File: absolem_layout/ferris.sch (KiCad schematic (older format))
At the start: 102 parts, among them J1 USB C, K0_0 KEYSW, K0_1 KEYSW, K0_2 KEYSW, K0_3 KEYSW, K0_4 KEYSW, K0_5 KEYSW, K0_6 KEYSW, K0_7 KEYSW, K0_8 KEYSW, K0_9 KEYSW, K1_0 KEYSW, K1_1 KEYSW, K1_2 KEYSW, K1_3 KEYSW, K1_4 KEYSW, K1_5 KEYSW, K1_6 KEYSW, K1_7 KEYSW, K1_8 KEYSW, K1_9 KEYSW, K2_0 KEYSW, K2_1 KEYSW, K2_2 KEYSW, K2_3 KEYSW, K2_4 KEYSW, K2_5 KEYSW, K2_6 KEYSW, K2_7 KEYSW, K2_8 KEYSW, K2_9 KEYSW, K3_2 KEYSW, K3_3 KEYSW, K3_4 KEYSW, K3_5 KEYSW, K3_6 KEYSW, K3_7 KEYSW, SW1 SW_PUSH, U1 ATmega32U4-AU, Y1 Crystal

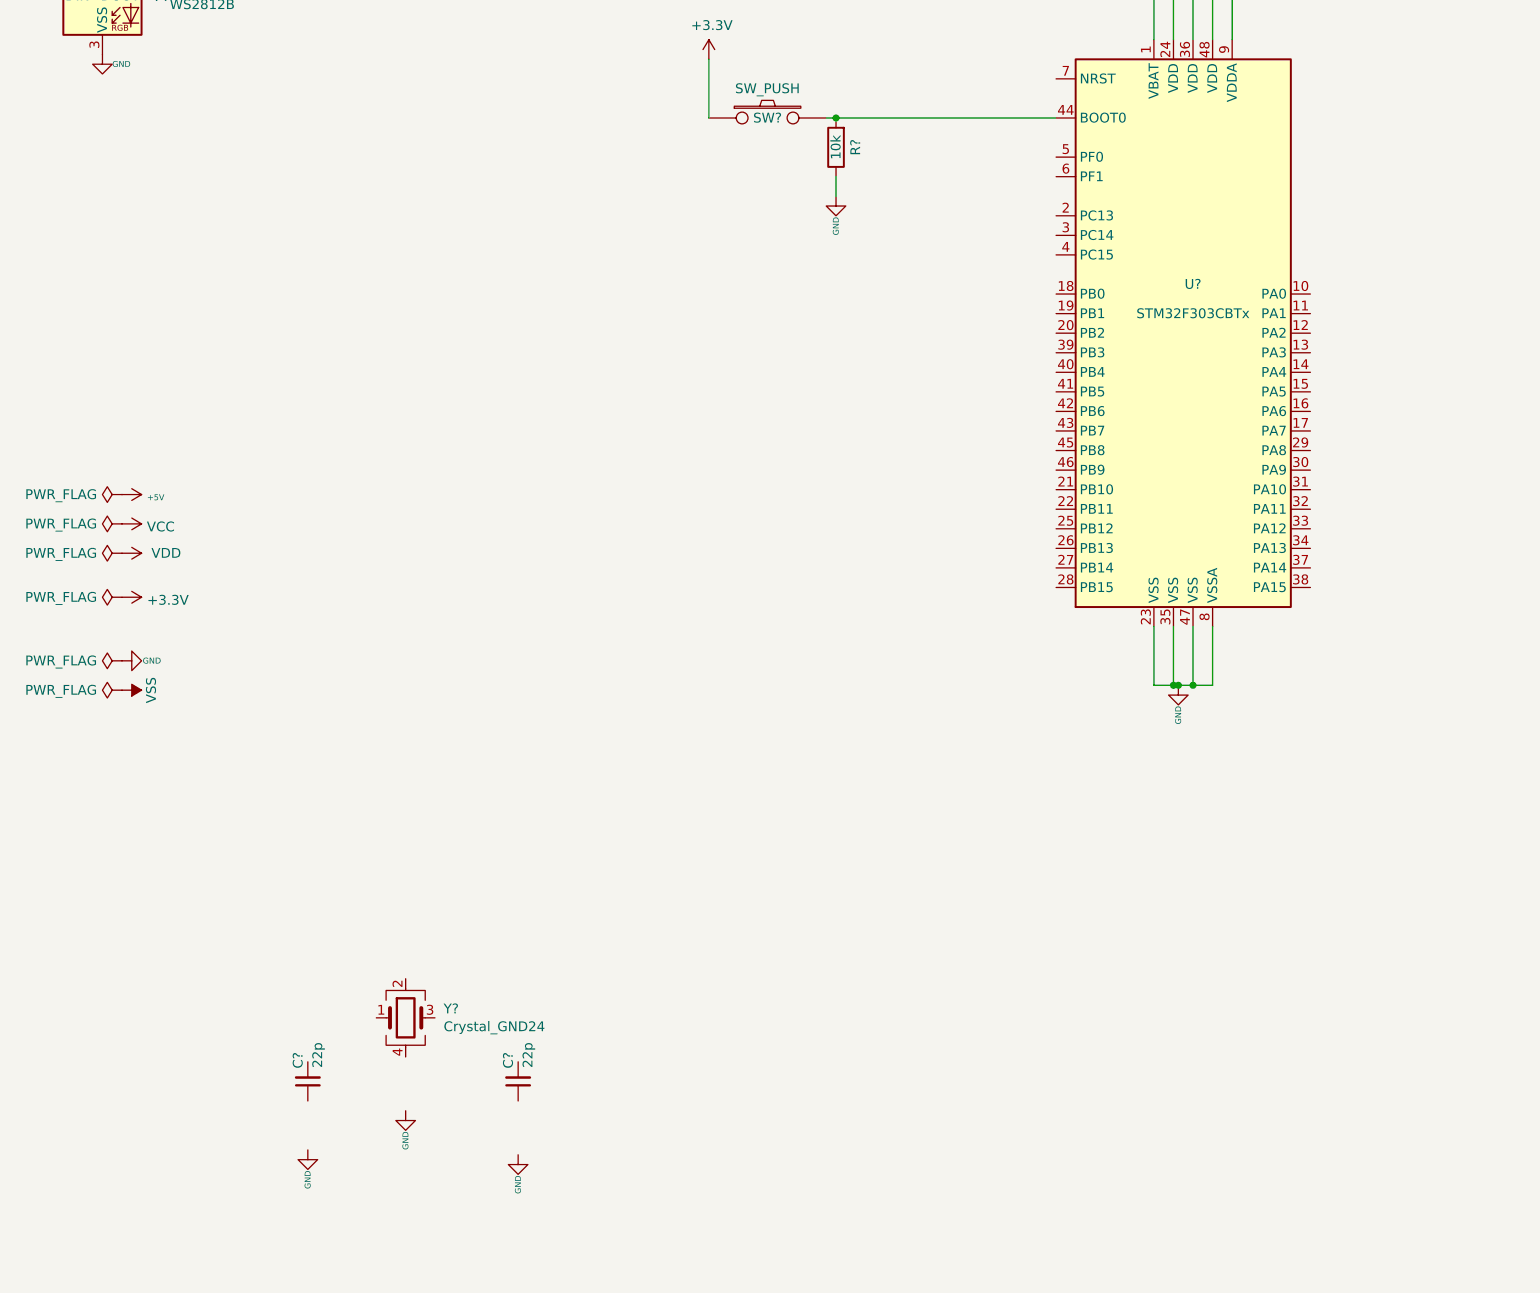
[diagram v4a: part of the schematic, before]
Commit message: Oscillator added to the schematic.
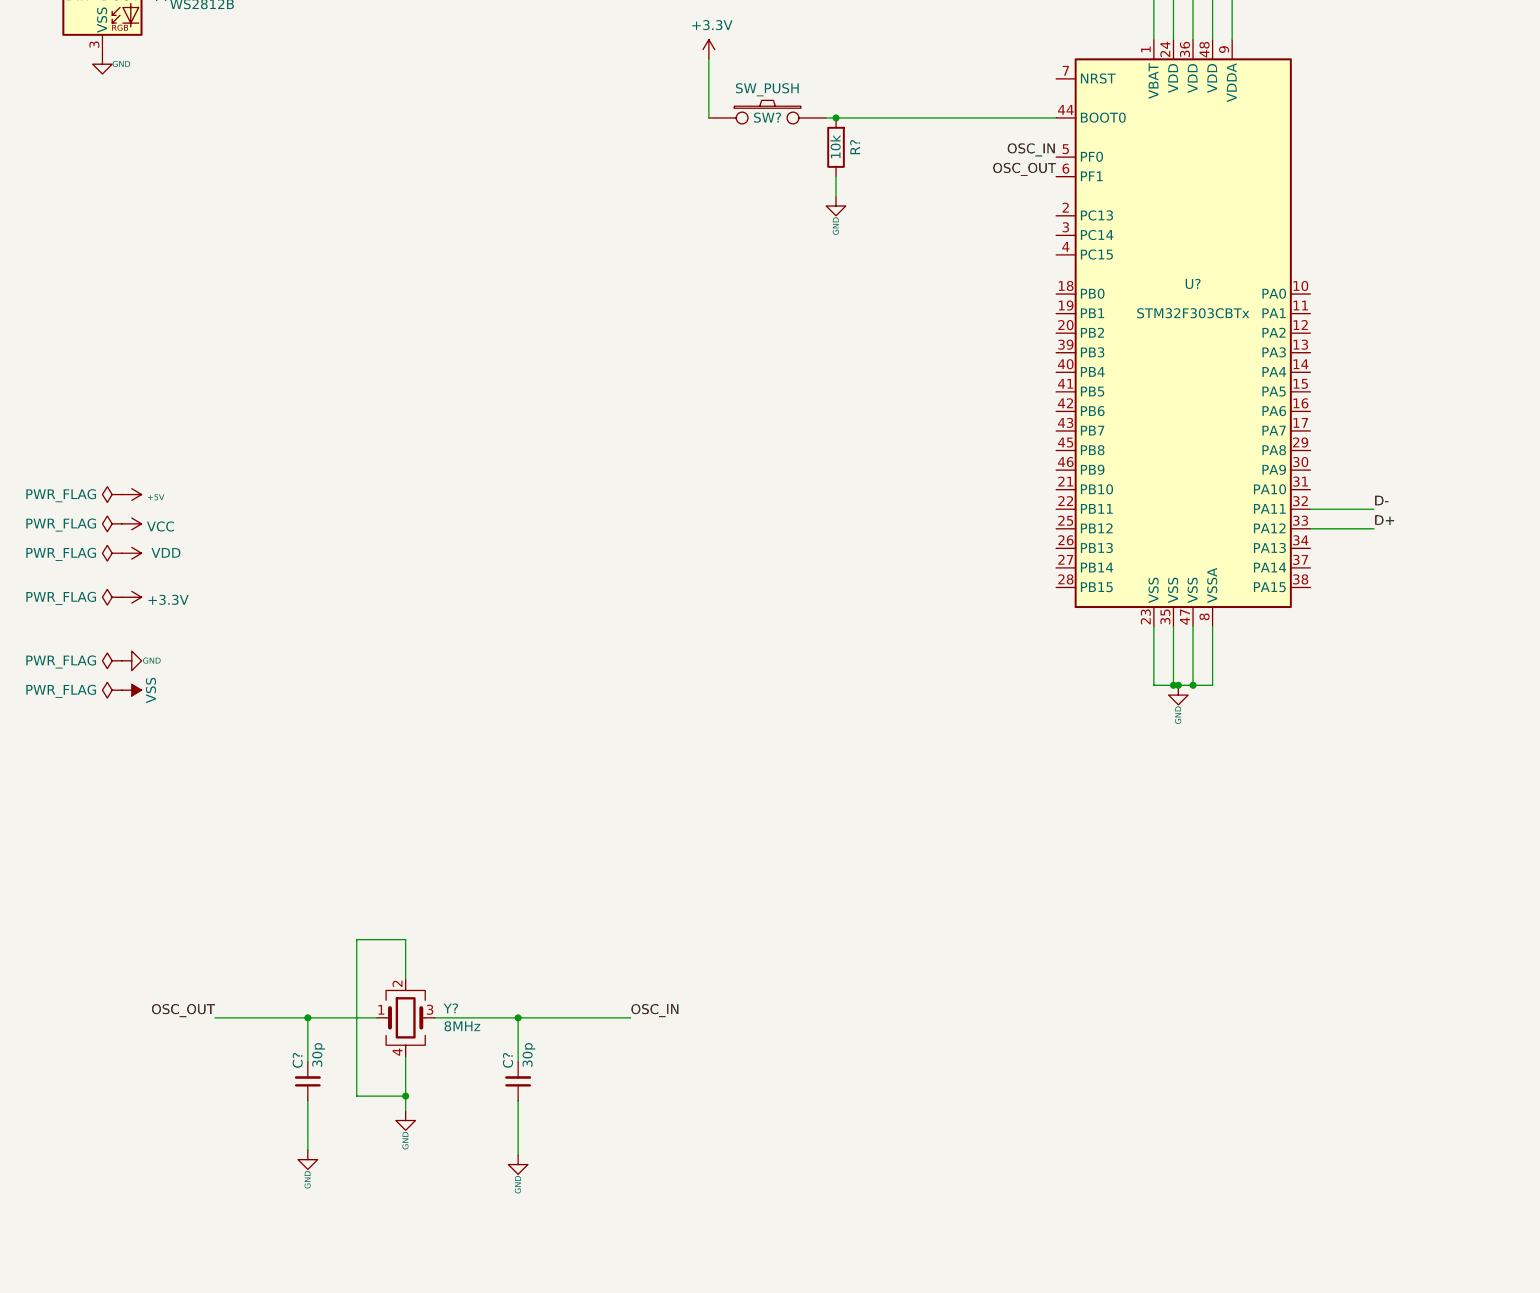
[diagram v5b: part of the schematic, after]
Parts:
- C? (x2): value 22p -> 30p
- Y?: value Crystal_GND24 -> 8MHz; footprint (none) -> Crystal:Crystal_SMD_5032-4Pin_5.0x3.2mm
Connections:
- net D+: now also U?.33 (PA12)
- net D-: now also U?.32 (PA11)
- net GND: now also C?.1, C?.1, Y?.2, Y?.4
- net OSC_IN: now reaches U?.5 (PF0)
- net OSC_IN: now also C?.2, Y?.3
- net OSC_OUT: now reaches U?.6 (PF1)
- net OSC_OUT: now also C?.2, Y?.1
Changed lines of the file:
@@
 P 6800 8925
 F 0 "Y?" H 6994 8971 50  0000 L CNN
-F 1 "Crystal_GND24" H 6994 8880 50  0000 L CNN
-F 2 "" H 6800 8925 50  0001 C CNN
+F 1 "8MHz" H 6994 8880 50  0000 L CNN
+F 2 "Crystal:Crystal_SMD_5032-4Pin_5.0x3.2mm" H 6800 8925 50  0001 C CNN
 F 3 "~" H 6800 8925 50  0001 C CNN
 	1    6800 8925
@@
 P 6300 9250
 F 0 "C?" V 6350 9100 50  0000 L CNN
-F 1 "22p" V 6250 9050 50  0000 L CNN
+F 1 "30p" V 6250 9050 50  0000 L CNN
 F 2 "Capacitor_SMD:C_0805_2012Metric_Pad1.15x1.40mm_HandSolder" H 6300 9250 50  0001 C CNN
 F 3 "~" H 6300 9250 50  0001 C CNN
@@
 P 7375 9250
 F 0 "C?" V 7425 9100 50  0000 L CNN
-F 1 "22p" V 7325 9050 50  0000 L CNN
+F 1 "30p" V 7325 9050 50  0000 L CNN
 F 2 "Capacitor_SMD:C_0805_2012Metric_Pad1.15x1.40mm_HandSolder" H 7375 9250 50  0001 C CNN
 F 3 "~" H 7375 9250 50  0001 C CNN
@@
 	1    0    0    -1
 $EndComp
+Text Label 10125 4525 2    50   ~ 0
+OSC_IN
+Text Label 10125 4625 2    50   ~ 0
+OSC_OUT
+Text Label 5825 8925 2    50   ~ 0
+OSC_OUT
+Text Label 7950 8925 0    50   ~ 0
+OSC_IN
+Wire Wire Line
+	7950 8925 7375 8925
+Wire Wire Line
+	6650 8925 6300 8925
+Wire Wire Line
+	6300 9150 6300 8925
+Connection ~ 6300 8925
+Wire Wire Line
+	6300 8925 5825 8925
+Wire Wire Line
+	6300 9350 6300 9600
+Wire Wire Line
+	7375 9150 7375 8925
+Connection ~ 7375 8925
+Wire Wire Line
+	7375 8925 6950 8925
+Wire Wire Line
+	7375 9350 7375 9625
+Wire Wire Line
+	6800 9125 6800 9325
+Wire Wire Line
+	6800 8725 6800 8525
+Wire Wire Line
+	6800 8525 6550 8525
+Wire Wire Line
+	6550 8525 6550 9325
+Wire Wire Line
+	6550 9325 6800 9325
+Connection ~ 6800 9325
+Wire Wire Line
+	6800 9325 6800 9400
+Text Label 11750 6425 0    50   ~ 0
+D+
+Text Label 11750 6325 0    50   ~ 0
+D-
+Wire Wire Line
+	11425 6325 11750 6325
+Wire Wire Line
+	11750 6425 11425 6425
 $EndSCHEMATC

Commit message: Labelling
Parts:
- gave numbers to parts that had none: 10
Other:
- note added: "EMI/RFI Filter unit"
- note added: "Oscillator unit"
- note added: "Voltage Regulator"
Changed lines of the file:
@@
 Connection ~ 3650 3900
 $Comp
-L NUF2221W1T2G:NUF2221W1T2G IC?
+L NUF2221W1T2G:NUF2221W1T2G IC1
 U 1 1 5F2F5E67
 P 1475 10250
-F 0 "IC?" H 1475 10250 50  0001 L BNN
+F 0 "IC1" H 1475 10250 50  0001 L BNN
 F 1 "NUF2221W1T2G" H 1475 10250 50  0001 L BNN
 F 2 "SOT-363" H 1475 10250 50  0001 L BNN
@@
 D-I
 $Comp
-L Regulator_Linear:TLV70012_SOT23-5 U?
+L Regulator_Linear:TLV70012_SOT23-5 U2
 U 1 1 5F305548
 P 3825 9875
-F 0 "U?" H 3825 10217 50  0000 C CNN
+F 0 "U2" H 3825 10217 50  0000 C CNN
 F 1 "TLV70012_SOT23-5" H 3825 10126 50  0000 C CNN
 F 2 "Package_TO_SOT_SMD:SOT-23-5" H 3825 10200 50  0001 C CIN
@@
 $EndComp
 $Comp
-L power:+5V #PWR?
+L power:+5V #PWR0106
 U 1 1 5F308B1A
 P 3200 9625
-F 0 "#PWR?" H 3200 9595 20  0001 C CNN
+F 0 "#PWR0106" H 3200 9595 20  0001 C CNN
 F 1 "+5V" V 3215 9753 30  0000 L CNN
 F 2 "" H 3200 9625 60  0000 C CNN
@@
 $EndComp
 $Comp
-L Device:C_Small C?
+L Device:C_Small C9
 U 1 1 5F3097C9
 P 3200 10250
-F 0 "C?" V 3100 10200 50  0000 L CNN
+F 0 "C9" V 3100 10200 50  0000 L CNN
 F 1 "1u" V 3300 10150 50  0000 L CNN
 F 2 "Capacitor_SMD:C_0805_2012Metric_Pad1.15x1.40mm_HandSolder" H 3200 10250 50  0001 C CNN
@@
 $EndComp
 $Comp
-L Device:C_Small C?
+L Device:C_Small C10
 U 1 1 5F30A45A
 P 4500 10225
-F 0 "C?" V 4400 10175 50  0000 L CNN
+F 0 "C10" V 4400 10175 50  0000 L CNN
 F 1 "1u" V 4600 10125 50  0000 L CNN
 F 2 "Capacitor_SMD:C_0805_2012Metric_Pad1.15x1.40mm_HandSolder" H 4500 10225 50  0001 C CNN
@@
 $EndComp
 $Comp
-L power:GND #PWR?
+L power:GND #PWR0112
 U 1 1 5F30ABDF
 P 3825 10725
-F 0 "#PWR?" H 3825 10775 20  0001 C CNN
+F 0 "#PWR0112" H 3825 10775 20  0001 C CNN
 F 1 "GND" V 3825 10525 30  0000 L CNN
 F 2 "" H 3825 10725 60  0000 C CNN
@@
 $EndComp
 $Comp
-L power:+3.3V #PWR?
+L power:+3.3V #PWR0117
 U 1 1 5F30C6C4
 P 5350 6775
-F 0 "#PWR?" H 5350 6625 50  0001 C CNN
+F 0 "#PWR0117" H 5350 6625 50  0001 C CNN
 F 1 "+3.3V" V 5365 6903 50  0000 L CNN
 F 2 "" H 5350 6775 50  0001 C CNN
@@
 $EndComp
 $Comp
-L power:PWR_FLAG #FLG?
+L power:PWR_FLAG #FLG0106
 U 1 1 5F30D7CC
 P 5350 6775
-F 0 "#FLG?" H 5350 6850 50  0001 C CNN
+F 0 "#FLG0106" H 5350 6850 50  0001 C CNN
 F 1 "PWR_FLAG" V 5350 6902 50  0000 L CNN
 F 2 "" H 5350 6775 50  0001 C CNN
@@
 $EndComp
 $Comp
-L power:+3.3V #PWR?
+L power:+3.3V #PWR0120
 U 1 1 5F30EBCB
 P 4500 9625
-F 0 "#PWR?" H 4500 9475 50  0001 C CNN
+F 0 "#PWR0120" H 4500 9475 50  0001 C CNN
 F 1 "+3.3V" H 4515 9798 50  0000 C CNN
 F 2 "" H 4500 9625 50  0001 C CNN
@@
 D-
 $Comp
-L power:+3.3V #PWR?
+L power:+3.3V #PWR0121
 U 1 1 5F335F51
 P 1075 10150
-F 0 "#PWR?" H 1075 10000 50  0001 C CNN
+F 0 "#PWR0121" H 1075 10000 50  0001 C CNN
 F 1 "+3.3V" V 1090 10278 50  0000 L CNN
 F 2 "" H 1075 10150 50  0001 C CNN
@@
 $EndComp
 $Comp
-L power:GND #PWR?
+L power:GND #PWR0123
 U 1 1 5F336B78
 P 1075 10650
-F 0 "#PWR?" H 1075 10700 20  0001 C CNN
+F 0 "#PWR0123" H 1075 10700 20  0001 C CNN
 F 1 "GND" V 1075 10450 30  0000 L CNN
 F 2 "" H 1075 10650 60  0000 C CNN
@@
 $EndComp
 $Comp
-L MCU_ST_STM32F3:STM32F303CBTx U?
+L MCU_ST_STM32F3:STM32F303CBTx U3
 U 1 1 5F2CE539
 P 10825 5425
-F 0 "U?" H 10825 5675 50  0000 C CNN
+F 0 "U3" H 10825 5675 50  0000 C CNN
 F 1 "STM32F303CBTx" H 10825 5525 50  0000 C CNN
 F 2 "Package_QFP:LQFP-48_7x7mm_P0.5mm" H 10225 4025 50  0001 R CNN
@@
 $EndComp
 $Comp
-L power:+3.3V #PWR?
+L power:+3.3V #PWR0124
 U 1 1 5F2D5F54
 P 10825 3500
-F 0 "#PWR?" H 10825 3350 50  0001 C CNN
+F 0 "#PWR0124" H 10825 3350 50  0001 C CNN
 F 1 "+3.3V" H 10840 3673 50  0000 C CNN
 F 2 "" H 10825 3500 50  0001 C CNN
@@
 Connection ~ 10725 3650
 $Comp
-L power:GND #PWR?
+L power:GND #PWR0125
 U 1 1 5F30895E
-P 10750 7225
-F 0 "#PWR?" H 10750 7275 20  0001 C CNN
-F 1 "GND" V 10750 7025 30  0000 L CNN
-F 2 "" H 10750 7225 60  0000 C CNN
-F 3 "" H 10750 7225 60  0000 C CNN
-	1    10750 7225
+P 10750 7400
+F 0 "#PWR0125" H 10750 7450 20  0001 C CNN
+F 1 "GND" V 10750 7200 30  0000 L CNN
+F 2 "" H 10750 7400 60  0000 C CNN
+F 3 "" H 10750 7400 60  0000 C CNN
+	1    10750 7400
 	1    0    0    -1
 $EndComp
@@
 	10825 7225 10750 7225
 $Comp
-L ferris-rescue:SW_PUSH-keyboard_parts-ferris-rescue SW?
+L ferris-rescue:SW_PUSH-keyboard_parts-ferris-rescue SW2
 U 1 1 5F33508A
 P 8650 4325
-F 0 "SW?" H 8650 4325 50  0000 C CNN
+F 0 "SW2" H 8650 4325 50  0000 C CNN
 F 1 "SW_PUSH" H 8650 4475 50  0000 C CNN
 F 2 "Button_Switch_SMD:SW_SPST_B3U-1000P" H 8650 4325 60  0001 C CNN
@@
 	10125 4325 9000 4325
 $Comp
-L power:+3.3V #PWR?
+L power:+3.3V #PWR0126
 U 1 1 5F346246
 P 8350 4025
-F 0 "#PWR?" H 8350 3875 50  0001 C CNN
+F 0 "#PWR0126" H 8350 3875 50  0001 C CNN
 F 1 "+3.3V" H 8365 4198 50  0000 C CNN
 F 2 "" H 8350 4025 50  0001 C CNN
@@
 	8350 4025 8350 4325
 $Comp
-L Device:R R?
+L Device:R R7
 U 1 1 5F355C69
 P 9000 4475
-F 0 "R?" V 8900 4475 50  0000 C CNN
+F 0 "R7" V 8900 4475 50  0000 C CNN
 F 1 "10k" V 9000 4475 50  0000 C CNN
 F 2 "Resistor_SMD:R_0805_2012Metric_Pad1.15x1.40mm_HandSolder" V 8930 4475 50  0001 C CNN
@@
 	9000 4325 8950 4325
 $Comp
-L power:GND #PWR?
+L power:GND #PWR0130
 U 1 1 5F359ECB
 P 9000 4725
-F 0 "#PWR?" H 9000 4775 20  0001 C CNN
+F 0 "#PWR0130" H 9000 4775 20  0001 C CNN
 F 1 "GND" V 9000 4525 30  0000 L CNN
 F 2 "" H 9000 4725 60  0000 C CNN
@@
 	9000 4625 9000 4725
 $Comp
-L Device:Crystal_GND24 Y?
+L Device:Crystal_GND24 Y2
 U 1 1 5F3648C6
 P 6800 8925
-F 0 "Y?" H 6994 8971 50  0000 L CNN
+F 0 "Y2" H 6994 8971 50  0000 L CNN
 F 1 "8MHz" H 6994 8880 50  0000 L CNN
 F 2 "Crystal:Crystal_SMD_5032-4Pin_5.0x3.2mm" H 6800 8925 50  0001 C CNN
@@
 $EndComp
 $Comp
-L Device:C_Small C?
+L Device:C_Small C11
 U 1 1 5F388BCB
 P 6300 9250
-F 0 "C?" V 6350 9100 50  0000 L CNN
+F 0 "C11" V 6350 9100 50  0000 L CNN
 F 1 "30p" V 6250 9050 50  0000 L CNN
 F 2 "Capacitor_SMD:C_0805_2012Metric_Pad1.15x1.40mm_HandSolder" H 6300 9250 50  0001 C CNN
@@
 $EndComp
 $Comp
-L Device:C_Small C?
+L Device:C_Small C12
 U 1 1 5F3901A1
 P 7375 9250
-F 0 "C?" V 7425 9100 50  0000 L CNN
+F 0 "C12" V 7425 9100 50  0000 L CNN
 F 1 "30p" V 7325 9050 50  0000 L CNN
 F 2 "Capacitor_SMD:C_0805_2012Metric_Pad1.15x1.40mm_HandSolder" H 7375 9250 50  0001 C CNN
@@
 $EndComp
 $Comp
-L power:GND #PWR?
+L power:GND #PWR0131
 U 1 1 5F391618
 P 6300 9600
-F 0 "#PWR?" H 6300 9650 20  0001 C CNN
+F 0 "#PWR0131" H 6300 9650 20  0001 C CNN
 F 1 "GND" V 6300 9400 30  0000 L CNN
 F 2 "" H 6300 9600 60  0000 C CNN
@@
 $EndComp
 $Comp
-L power:GND #PWR?
+L power:GND #PWR0132
 U 1 1 5F392713
 P 7375 9625
-F 0 "#PWR?" H 7375 9675 20  0001 C CNN
+F 0 "#PWR0132" H 7375 9675 20  0001 C CNN
 F 1 "GND" V 7375 9425 30  0000 L CNN
 F 2 "" H 7375 9625 60  0000 C CNN
@@
 $EndComp
 $Comp
-L power:GND #PWR?
+L power:GND #PWR0133
 U 1 1 5F392D31
 P 6800 9400
-F 0 "#PWR?" H 6800 9450 20  0001 C CNN
+F 0 "#PWR0133" H 6800 9450 20  0001 C CNN
 F 1 "GND" V 6800 9200 30  0000 L CNN
 F 2 "" H 6800 9400 60  0000 C CNN
@@
 Wire Wire Line
 	11750 6425 11425 6425
+Text Notes 4100 11075 2    50   ~ 0
+Voltage Regulator
+Text Notes 1750 11000 2    50   ~ 0
+EMI/RFI Filter unit
+Text Notes 7075 9875 2    50   ~ 0
+Oscillator unit
+Wire Wire Line
+	10750 7400 10750 7225
 $EndSCHEMATC

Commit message: Deivid changes.
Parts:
- added C?: 100n, Capacitor_SMD:C_0805_2012Metric_Pad1.15x1.40mm_HandSolder, symbol ferris-rescue:C_Small-Device
- C1, C10, C11, C12, C2, C3, C4, C5, C6, C7, C8, C9: symbol Device:C_Small -> ferris-rescue:C_Small-Device
- D0_0, D0_1, D0_2, D0_3, D0_4, D0_5, D0_6, D0_7, D0_8, D0_9, D1_0, D1_1, D1_2, D1_3, D1_4, D1_5, D1_6, D1_7, D1_8, D1_9, D2_0, D2_1, D2_2, D2_3, D2_4, D2_5, D2_6, D2_7, D2_8, D2_9, D3_2, D3_3, D3_4, D3_5, D3_6, D3_7: symbol Device:D -> ferris-rescue:D-Device
- D1: symbol LED:WS2812B -> ferris-rescue:WS2812B-LED
- F1: symbol Device:Polyfuse -> ferris-rescue:Polyfuse-Device
- J1: symbol Connector:USB_C_Receptacle_USB2.0 -> ferris-rescue:USB_C_Receptacle_USB2.0-Connector
- R1, R2, R3, R4, R5, R6, R7: symbol Device:R -> ferris-rescue:R-Device
- U1: symbol MCU_Microchip_ATmega:ATmega32U4-AU -> ferris-rescue:ATmega32U4-AU-MCU_Microchip_ATmega
- U2: symbol Regulator_Linear:TLV70012_SOT23-5 -> ferris-rescue:TLV70012_SOT23-5-Regulator_Linear
- U3: symbol MCU_ST_STM32F3:STM32F303CBTx -> ferris-rescue:STM32F303CBTx-MCU_ST_STM32F3
- Y1: symbol Device:Crystal_GND24_Small -> ferris-rescue:Crystal_GND24_Small-Device
- Y2: symbol Device:Crystal_GND24 -> ferris-rescue:Crystal_GND24-Device
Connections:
- net GND: now also C?.2
- net at U3.7 (NRST): now also C?.1
- net row0,0 renamed row0
- net row0,1 renamed row1
- net row0,2 renamed row2
- net row0,3 renamed row3
